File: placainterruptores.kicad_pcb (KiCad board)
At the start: 2 copper layers, 49.5 x 99.7 mm, 72 parts, among them P10 CONN_2, P11 CONN_2, P12 CONN_2, P13 CONN_2, P14 CONN_2, P15 CONN_2, P16 CONN_2, P17 CONN_2, P2 CONN_2, P3 CONN_2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

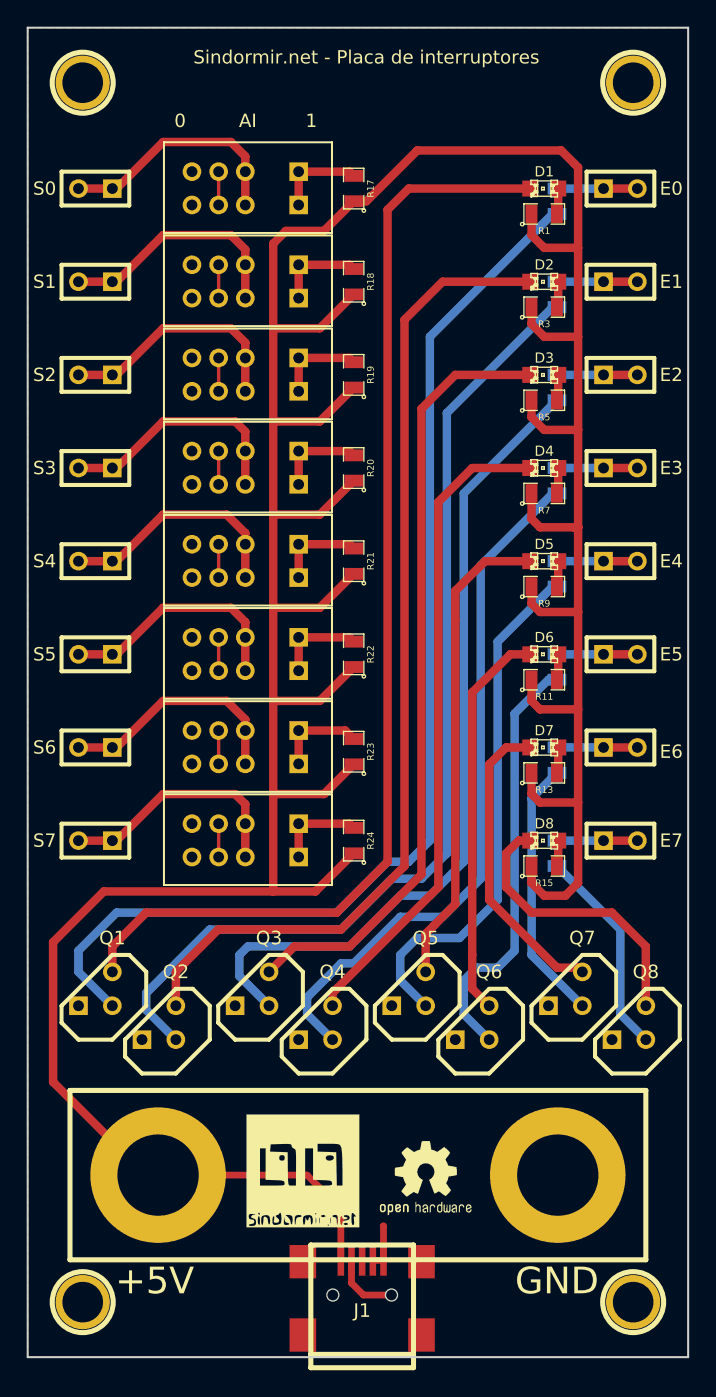
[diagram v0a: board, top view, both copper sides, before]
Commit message: Ahora no hay que pasar por HiZ para ir desde 5V a GND, lo que mejora la generación de flancos de subida/bajada. Placa adaptada para la nueva versión de Kicad. Nuevos ficheros de fabricación generados
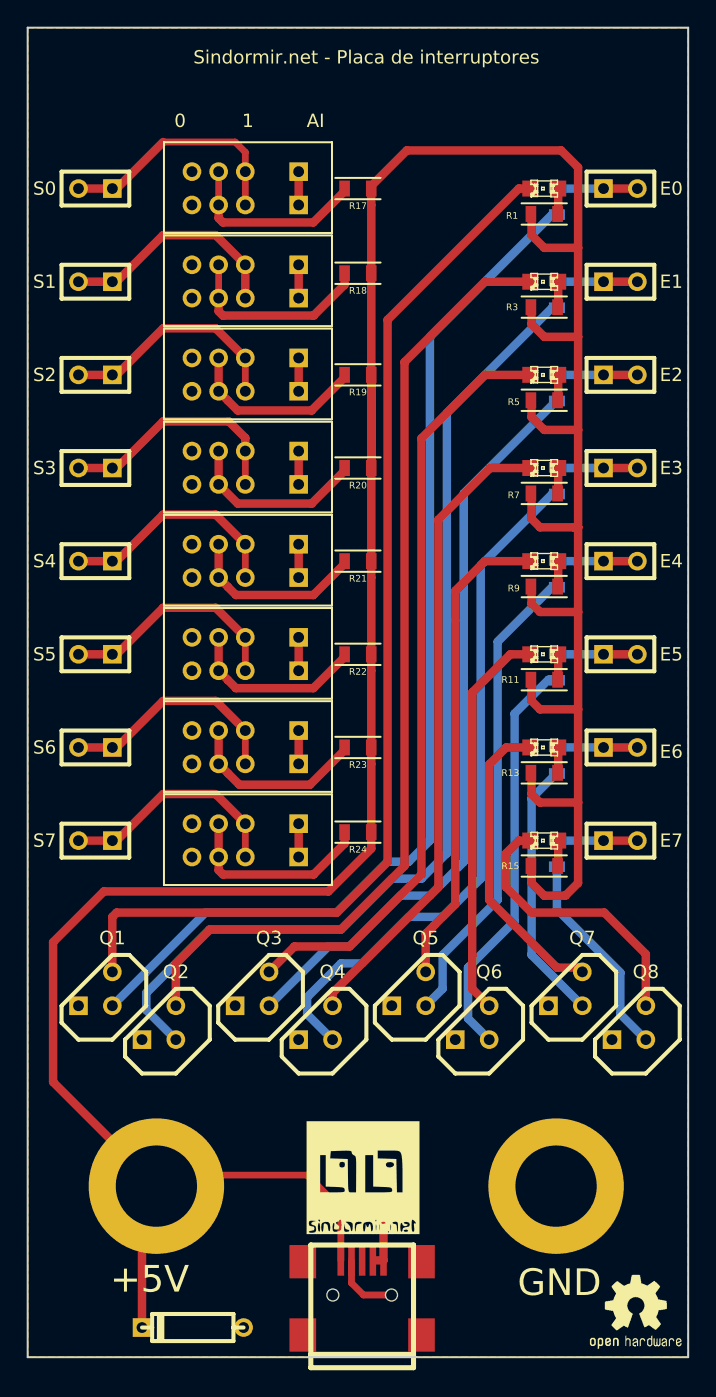
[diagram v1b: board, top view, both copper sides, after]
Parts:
- removed ?: , 2PIN_6mm
- removed ?: 3WAY_SWITCH, 3WAY-SWITCH
- removed ? (x2): , 1pin
- removed ? (x2): P***, 1pin
- removed the G*** at (95.6, 146.1)
- removed the G*** at (101.0, 142.9)
- added D9: DIODE, Discret:D3, F.Cu at (87.3, 157.8)
- added G***: LOGO, LOGOSD:LOGO, F.Cu at (100.1, 146.6)
- added G***: LOGO, LOGOOH:OSHWLOGO0.3IN, F.Cu at (116.7, 152.9)
- added P1: CONN_2, Divers:2PIN_6mm, F.Cu at (99.6, 147.2)
- added SW8: 3WAY_SWITCH, PI2:3WAY-SWITCH, F.Cu at (95.2, 120.0)
- D1, D2, D3, D4, D5, D6, D7, D8: footprint LED-0805 -> LEDs:LED-0805
- J1: value (none) -> USB; footprint USB_MINI_B -> Connect:USB_MINI_B
- P10, P11, P12, P13, P14, P15, P16, P17, P2, P3, P4, P5, P6, P7, P8, P9: footprint SIL-2 -> Connect:SIL-2
- Q1, Q2, Q3, Q4, Q5, Q6, Q7, Q8: value (none) -> BC547; footprint TO92-123 -> Discret:TO92-123
- R1, R10, R11, R12, R13, R14, R15, R16, R17, R18, R19, R2, R20, R21, R22, R23, R24, R3, R4, R5, R6, R7, R8, R9: footprint SM0805 -> Resistors_SMD:R_0805
- SW1, SW2, SW3, SW4, SW5, SW6, SW7: footprint 3WAY-SWITCH -> PI2:3WAY-SWITCH
- moved R18 0.71 mm to (99.7, 78.7), turned to 180 degrees
- moved R24 0.71 mm to (99.7, 120.7), turned to 180 degrees
- moved R23 0.45 mm to (99.7, 114.3), turned to 180 degrees
- moved R17 0.32 mm to (99.7, 72.4), turned to 180 degrees
- moved R19 0.32 mm to (99.7, 86.4), turned to 180 degrees
- moved R20 0.32 mm to (99.7, 93.3), turned to 180 degrees
- moved R21 0.32 mm to (99.7, 100.3), turned to 180 degrees
- moved R22 0.32 mm to (99.7, 107.3), turned to 180 degrees
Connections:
- J1 pad 3: N-0000028 -> (no net)
- R17 pad 2: N-0000012 -> Net-(R17-Pad2)
- R18 pad 2: N-0000010 -> Net-(R18-Pad2)
- R19 pad 2: N-0000018 -> Net-(R19-Pad2)
- R20 pad 2: N-000005 -> Net-(R20-Pad2)
- R21 pad 2: N-000001 -> Net-(R21-Pad2)
- R22 pad 2: N-000007 -> Net-(R22-Pad2)
- R23 pad 2: N-0000026 -> Net-(R23-Pad2)
- SW1 pad 1: N-0000012 -> Net-(SW1-Pad1)
- SW1 pad 3: N-0000031 -> Net-(R17-Pad2)
- SW2 pad 1: N-0000010 -> Net-(SW2-Pad1)
- SW2 pad 3: N-0000025 -> Net-(R18-Pad2)
- SW3 pad 1: N-0000018 -> Net-(SW3-Pad1)
- SW3 pad 3: N-0000020 -> Net-(R19-Pad2)
- SW4 pad 1: N-000005 -> Net-(SW4-Pad1)
- SW4 pad 3: N-0000021 -> Net-(R20-Pad2)
- SW5 pad 1: N-000001 -> Net-(SW5-Pad1)
- SW5 pad 3: N-0000022 -> Net-(R21-Pad2)
- SW6 pad 1: N-000007 -> Net-(SW6-Pad1)
- SW6 pad 3: N-0000023 -> Net-(R22-Pad2)
- SW7 pad 1: N-0000026 -> Net-(SW7-Pad1)
- SW7 pad 3: N-0000019 -> Net-(R23-Pad2)
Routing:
- net +5V: track 279.4 -> 249.0 mm
- net Net-(R18-Pad2): track 0.00 -> 14.9 mm
- net Net-(R17-Pad2): track 0.00 -> 14.2 mm
- net Net-(R23-Pad2): track 0.00 -> 13.9 mm
- net Net-(R19-Pad2): track 0.00 -> 13.8 mm
- net Net-(R20-Pad2): track 0.00 -> 13.8 mm
- net Net-(R22-Pad2): track 0.00 -> 13.7 mm
- net Net-(R21-Pad2): track 0.00 -> 13.7 mm
- net Net-(R24-Pad2): track 6.76 -> 14.9 mm
- net N-0000026: track 6.89 -> 0.00 mm
- net N-000007: track 6.76 -> 0.00 mm
- net N-000005: track 6.76 -> 0.00 mm
- net N-0000018: track 6.76 -> 0.00 mm
- net N-0000012: track 6.76 -> 0.00 mm
- net N-0000010: track 6.76 -> 0.00 mm
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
